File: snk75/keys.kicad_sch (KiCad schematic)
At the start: 255 parts

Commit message: Began routing
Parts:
- renumbered R12 to R10, R13 to R11, R14 to R12, R15 to R13, R16 to R14, R17 to R15, R18 to R16, R19 to R17, R20 to R18, R21 to R19, R22 to R20, R23 to R21, R24 to R22, R25 to R23, R26 to R24, R27 to R25, R28 to R26, R29 to R27, R30 to R28, R31 to R29, R32 to R30, R33 to R31, R34 to R32, R35 to R33, R36 to R34, R37 to R35, R38 to R36, R39 to R37, R40 to R38, R41 to R39, R42 to R40, R43 to R41, R44 to R42, R45 to R43, R46 to R44, R47 to R45, R48 to R46, R49 to R47, R50 to R48, R51 to R49, R52 to R50, R53 to R51, R54 to R52, R55 to R53, R56 to R54, R57 to R55, R58 to R56, R59 to R57, R60 to R58, R61 to R59, R62 to R60, R63 to R61, R64 to R62, R65 to R63, R66 to R64, R67 to R65, R68 to R66, R69 to R67, R70 to R68, R71 to R69, R72 to R70, R73 to R71, R74 to R72, R75 to R73, R76 to R74, R77 to R75, R78 to R76, R79 to R77, R80 to R78, R81 to R79, R10 to R8, R82 to R80, R83 to R81, R84 to R82, R85 to R83, R86 to R84, R87 to R85, R88 to R86, R89 to R87, R90 to R88, R91 to R89, R11 to R9, R92 to R90, R93 to R91, R94 to R92
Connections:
- net row1: no longer D7.1 (K)
- net at D7.2 (A): no longer MX7.2 (ROW)
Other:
- moved on the sheet: D7

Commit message: Changed MCU for STM32F072C8Tx and wired cols and rows
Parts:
- D1, D10, D11, D12, D13, D14, D15, D16, D17, D18, D19, D2, D20, D21, D22, D23, D24, D25, D26, D27, D28, D29, D3, D30, D31, D32, D33, D34, D35, D36, D37, D38, D39, D4, D40, D41, D42, D43, D44, D45, D46, D47, D48, D49, D5, D50, D51, D52, D53, D54, D55, D56, D57, D58, D59, D6, D60, D61, D62, D63, D64, D65, D66, D67, D68, D69, D7, D70, D71, D72, D73, D74, D75, D76, D77, D78, D79, D8, D80, D81, D82, D83, D84, D85, D9: footprint Diode_SMD:D_SOD-123 -> acheron_Components:D_SOD-123
- R10: renamed from R14; footprint Resistor_SMD:R_1206_3216Metric_Pad1.30x1.75mm_HandSolder -> Resistor_SMD:R_0402_1005Metric
- R11: renamed from R15; footprint Resistor_SMD:R_1206_3216Metric_Pad1.30x1.75mm_HandSolder -> Resistor_SMD:R_0402_1005Metric
- R12: renamed from R16; footprint Resistor_SMD:R_1206_3216Metric_Pad1.30x1.75mm_HandSolder -> Resistor_SMD:R_0402_1005Metric
- R13: renamed from R17; footprint Resistor_SMD:R_1206_3216Metric_Pad1.30x1.75mm_HandSolder -> Resistor_SMD:R_0402_1005Metric
- R14: renamed from R18; footprint Resistor_SMD:R_1206_3216Metric_Pad1.30x1.75mm_HandSolder -> Resistor_SMD:R_0402_1005Metric
- R15: renamed from R19; footprint Resistor_SMD:R_1206_3216Metric_Pad1.30x1.75mm_HandSolder -> Resistor_SMD:R_0402_1005Metric
- R16: renamed from R20; footprint Resistor_SMD:R_1206_3216Metric_Pad1.30x1.75mm_HandSolder -> Resistor_SMD:R_0402_1005Metric
- R17: renamed from R21; footprint Resistor_SMD:R_1206_3216Metric_Pad1.30x1.75mm_HandSolder -> Resistor_SMD:R_0402_1005Metric
- R18: renamed from R22; footprint Resistor_SMD:R_1206_3216Metric_Pad1.30x1.75mm_HandSolder -> Resistor_SMD:R_0402_1005Metric
- R19: renamed from R23; footprint Resistor_SMD:R_1206_3216Metric_Pad1.30x1.75mm_HandSolder -> Resistor_SMD:R_0402_1005Metric
- R20: renamed from R24; footprint Resistor_SMD:R_1206_3216Metric_Pad1.30x1.75mm_HandSolder -> Resistor_SMD:R_0402_1005Metric
- R21: renamed from R25; footprint Resistor_SMD:R_1206_3216Metric_Pad1.30x1.75mm_HandSolder -> Resistor_SMD:R_0402_1005Metric
- R22: renamed from R26; footprint Resistor_SMD:R_1206_3216Metric_Pad1.30x1.75mm_HandSolder -> Resistor_SMD:R_0402_1005Metric
- R23: renamed from R27; footprint Resistor_SMD:R_1206_3216Metric_Pad1.30x1.75mm_HandSolder -> Resistor_SMD:R_0402_1005Metric
- R24: renamed from R28; footprint Resistor_SMD:R_1206_3216Metric_Pad1.30x1.75mm_HandSolder -> Resistor_SMD:R_0402_1005Metric
- R25: renamed from R29; footprint Resistor_SMD:R_1206_3216Metric_Pad1.30x1.75mm_HandSolder -> Resistor_SMD:R_0402_1005Metric
- R26: renamed from R30; footprint Resistor_SMD:R_1206_3216Metric_Pad1.30x1.75mm_HandSolder -> Resistor_SMD:R_0402_1005Metric
- R27: renamed from R31; footprint Resistor_SMD:R_1206_3216Metric_Pad1.30x1.75mm_HandSolder -> Resistor_SMD:R_0402_1005Metric
- R28: renamed from R32; footprint Resistor_SMD:R_1206_3216Metric_Pad1.30x1.75mm_HandSolder -> Resistor_SMD:R_0402_1005Metric
- R29: renamed from R33; footprint Resistor_SMD:R_1206_3216Metric_Pad1.30x1.75mm_HandSolder -> Resistor_SMD:R_0402_1005Metric
- R30: renamed from R34; footprint Resistor_SMD:R_1206_3216Metric_Pad1.30x1.75mm_HandSolder -> Resistor_SMD:R_0402_1005Metric
- R31: renamed from R35; footprint Resistor_SMD:R_1206_3216Metric_Pad1.30x1.75mm_HandSolder -> Resistor_SMD:R_0402_1005Metric
- R32: renamed from R36; footprint Resistor_SMD:R_1206_3216Metric_Pad1.30x1.75mm_HandSolder -> Resistor_SMD:R_0402_1005Metric
- R33: renamed from R37; footprint Resistor_SMD:R_1206_3216Metric_Pad1.30x1.75mm_HandSolder -> Resistor_SMD:R_0402_1005Metric
- R34: renamed from R38; footprint Resistor_SMD:R_1206_3216Metric_Pad1.30x1.75mm_HandSolder -> Resistor_SMD:R_0402_1005Metric
- R35: renamed from R39; footprint Resistor_SMD:R_1206_3216Metric_Pad1.30x1.75mm_HandSolder -> Resistor_SMD:R_0402_1005Metric
- R36: renamed from R40; footprint Resistor_SMD:R_1206_3216Metric_Pad1.30x1.75mm_HandSolder -> Resistor_SMD:R_0402_1005Metric
- R37: renamed from R41; footprint Resistor_SMD:R_1206_3216Metric_Pad1.30x1.75mm_HandSolder -> Resistor_SMD:R_0402_1005Metric
- R38: renamed from R42; footprint Resistor_SMD:R_1206_3216Metric_Pad1.30x1.75mm_HandSolder -> Resistor_SMD:R_0402_1005Metric
- R39: renamed from R43; footprint Resistor_SMD:R_1206_3216Metric_Pad1.30x1.75mm_HandSolder -> Resistor_SMD:R_0402_1005Metric
- R4: renamed from R8; footprint Resistor_SMD:R_1206_3216Metric_Pad1.30x1.75mm_HandSolder -> Resistor_SMD:R_0402_1005Metric
- R40: renamed from R44; footprint Resistor_SMD:R_1206_3216Metric_Pad1.30x1.75mm_HandSolder -> Resistor_SMD:R_0402_1005Metric
- R41: renamed from R45; footprint Resistor_SMD:R_1206_3216Metric_Pad1.30x1.75mm_HandSolder -> Resistor_SMD:R_0402_1005Metric
- R42: renamed from R46; footprint Resistor_SMD:R_1206_3216Metric_Pad1.30x1.75mm_HandSolder -> Resistor_SMD:R_0402_1005Metric
- R43: renamed from R47; footprint Resistor_SMD:R_1206_3216Metric_Pad1.30x1.75mm_HandSolder -> Resistor_SMD:R_0402_1005Metric
- R44: renamed from R48; footprint Resistor_SMD:R_1206_3216Metric_Pad1.30x1.75mm_HandSolder -> Resistor_SMD:R_0402_1005Metric
- R45: renamed from R49; footprint Resistor_SMD:R_1206_3216Metric_Pad1.30x1.75mm_HandSolder -> Resistor_SMD:R_0402_1005Metric
- R46: renamed from R50; footprint Resistor_SMD:R_1206_3216Metric_Pad1.30x1.75mm_HandSolder -> Resistor_SMD:R_0402_1005Metric
- R47: renamed from R51; footprint Resistor_SMD:R_1206_3216Metric_Pad1.30x1.75mm_HandSolder -> Resistor_SMD:R_0402_1005Metric
- R48: renamed from R52; footprint Resistor_SMD:R_1206_3216Metric_Pad1.30x1.75mm_HandSolder -> Resistor_SMD:R_0402_1005Metric
- R49: renamed from R53; footprint Resistor_SMD:R_1206_3216Metric_Pad1.30x1.75mm_HandSolder -> Resistor_SMD:R_0402_1005Metric
- R5: renamed from R9; footprint Resistor_SMD:R_1206_3216Metric_Pad1.30x1.75mm_HandSolder -> Resistor_SMD:R_0402_1005Metric
- R50: renamed from R54; footprint Resistor_SMD:R_1206_3216Metric_Pad1.30x1.75mm_HandSolder -> Resistor_SMD:R_0402_1005Metric
- R51: renamed from R55; footprint Resistor_SMD:R_1206_3216Metric_Pad1.30x1.75mm_HandSolder -> Resistor_SMD:R_0402_1005Metric
- R52: renamed from R56; footprint Resistor_SMD:R_1206_3216Metric_Pad1.30x1.75mm_HandSolder -> Resistor_SMD:R_0402_1005Metric
- R53: renamed from R57; footprint Resistor_SMD:R_1206_3216Metric_Pad1.30x1.75mm_HandSolder -> Resistor_SMD:R_0402_1005Metric
- R54: renamed from R58; footprint Resistor_SMD:R_1206_3216Metric_Pad1.30x1.75mm_HandSolder -> Resistor_SMD:R_0402_1005Metric
- R55: renamed from R59; footprint Resistor_SMD:R_1206_3216Metric_Pad1.30x1.75mm_HandSolder -> Resistor_SMD:R_0402_1005Metric
- R56: renamed from R60; footprint Resistor_SMD:R_1206_3216Metric_Pad1.30x1.75mm_HandSolder -> Resistor_SMD:R_0402_1005Metric
- R57: renamed from R61; footprint Resistor_SMD:R_1206_3216Metric_Pad1.30x1.75mm_HandSolder -> Resistor_SMD:R_0402_1005Metric
- R58: renamed from R62; footprint Resistor_SMD:R_1206_3216Metric_Pad1.30x1.75mm_HandSolder -> Resistor_SMD:R_0402_1005Metric
- R59: renamed from R63; footprint Resistor_SMD:R_1206_3216Metric_Pad1.30x1.75mm_HandSolder -> Resistor_SMD:R_0402_1005Metric
- R6: renamed from R10; footprint Resistor_SMD:R_1206_3216Metric_Pad1.30x1.75mm_HandSolder -> Resistor_SMD:R_0402_1005Metric
- R60: renamed from R64; footprint Resistor_SMD:R_1206_3216Metric_Pad1.30x1.75mm_HandSolder -> Resistor_SMD:R_0402_1005Metric
- R61: renamed from R65; footprint Resistor_SMD:R_1206_3216Metric_Pad1.30x1.75mm_HandSolder -> Resistor_SMD:R_0402_1005Metric
- R62: renamed from R66; footprint Resistor_SMD:R_1206_3216Metric_Pad1.30x1.75mm_HandSolder -> Resistor_SMD:R_0402_1005Metric
- R63: renamed from R67; footprint Resistor_SMD:R_1206_3216Metric_Pad1.30x1.75mm_HandSolder -> Resistor_SMD:R_0402_1005Metric
- R64: renamed from R68; footprint Resistor_SMD:R_1206_3216Metric_Pad1.30x1.75mm_HandSolder -> Resistor_SMD:R_0402_1005Metric
- R65: renamed from R69; footprint Resistor_SMD:R_1206_3216Metric_Pad1.30x1.75mm_HandSolder -> Resistor_SMD:R_0402_1005Metric
- R66: renamed from R70; footprint Resistor_SMD:R_1206_3216Metric_Pad1.30x1.75mm_HandSolder -> Resistor_SMD:R_0402_1005Metric
- R67: renamed from R71; footprint Resistor_SMD:R_1206_3216Metric_Pad1.30x1.75mm_HandSolder -> Resistor_SMD:R_0402_1005Metric
- R68: renamed from R72; footprint Resistor_SMD:R_1206_3216Metric_Pad1.30x1.75mm_HandSolder -> Resistor_SMD:R_0402_1005Metric
- R69: renamed from R73; footprint Resistor_SMD:R_1206_3216Metric_Pad1.30x1.75mm_HandSolder -> Resistor_SMD:R_0402_1005Metric
- R7: renamed from R11; footprint Resistor_SMD:R_1206_3216Metric_Pad1.30x1.75mm_HandSolder -> Resistor_SMD:R_0402_1005Metric
- R70: renamed from R74; footprint Resistor_SMD:R_1206_3216Metric_Pad1.30x1.75mm_HandSolder -> Resistor_SMD:R_0402_1005Metric
- R71: renamed from R75; footprint Resistor_SMD:R_1206_3216Metric_Pad1.30x1.75mm_HandSolder -> Resistor_SMD:R_0402_1005Metric
- R72: renamed from R76; footprint Resistor_SMD:R_1206_3216Metric_Pad1.30x1.75mm_HandSolder -> Resistor_SMD:R_0402_1005Metric
- R73: renamed from R77; footprint Resistor_SMD:R_1206_3216Metric_Pad1.30x1.75mm_HandSolder -> Resistor_SMD:R_0402_1005Metric
- R74: renamed from R78; footprint Resistor_SMD:R_1206_3216Metric_Pad1.30x1.75mm_HandSolder -> Resistor_SMD:R_0402_1005Metric
- R75: renamed from R79; footprint Resistor_SMD:R_1206_3216Metric_Pad1.30x1.75mm_HandSolder -> Resistor_SMD:R_0402_1005Metric
- R76: renamed from R80; footprint Resistor_SMD:R_1206_3216Metric_Pad1.30x1.75mm_HandSolder -> Resistor_SMD:R_0402_1005Metric
- R77: renamed from R81; footprint Resistor_SMD:R_1206_3216Metric_Pad1.30x1.75mm_HandSolder -> Resistor_SMD:R_0402_1005Metric
- R78: renamed from R82; footprint Resistor_SMD:R_1206_3216Metric_Pad1.30x1.75mm_HandSolder -> Resistor_SMD:R_0402_1005Metric
- R79: renamed from R83; footprint Resistor_SMD:R_1206_3216Metric_Pad1.30x1.75mm_HandSolder -> Resistor_SMD:R_0402_1005Metric
- R8: renamed from R12; footprint Resistor_SMD:R_1206_3216Metric_Pad1.30x1.75mm_HandSolder -> Resistor_SMD:R_0402_1005Metric
- R80: renamed from R84; footprint Resistor_SMD:R_1206_3216Metric_Pad1.30x1.75mm_HandSolder -> Resistor_SMD:R_0402_1005Metric
- R81: renamed from R85; footprint Resistor_SMD:R_1206_3216Metric_Pad1.30x1.75mm_HandSolder -> Resistor_SMD:R_0402_1005Metric
- R82: renamed from R86; footprint Resistor_SMD:R_1206_3216Metric_Pad1.30x1.75mm_HandSolder -> Resistor_SMD:R_0402_1005Metric
- R83: renamed from R87; footprint Resistor_SMD:R_1206_3216Metric_Pad1.30x1.75mm_HandSolder -> Resistor_SMD:R_0402_1005Metric
- R84: renamed from R88; footprint Resistor_SMD:R_1206_3216Metric_Pad1.30x1.75mm_HandSolder -> Resistor_SMD:R_0402_1005Metric
- R85: renamed from R89; footprint Resistor_SMD:R_1206_3216Metric_Pad1.30x1.75mm_HandSolder -> Resistor_SMD:R_0402_1005Metric
- R86: renamed from R90; footprint Resistor_SMD:R_1206_3216Metric_Pad1.30x1.75mm_HandSolder -> Resistor_SMD:R_0402_1005Metric
- R87: renamed from R91; footprint Resistor_SMD:R_1206_3216Metric_Pad1.30x1.75mm_HandSolder -> Resistor_SMD:R_0402_1005Metric
- R88: renamed from R92; footprint Resistor_SMD:R_1206_3216Metric_Pad1.30x1.75mm_HandSolder -> Resistor_SMD:R_0402_1005Metric
- R9: renamed from R13; footprint Resistor_SMD:R_1206_3216Metric_Pad1.30x1.75mm_HandSolder -> Resistor_SMD:R_0402_1005Metric
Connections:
- net col15: now also MX82.1 (COL)
- net row1: now also D7.1 (K)
- net at D7.2 (A): now also MX7.2 (ROW)
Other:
- moved on the sheet: D7

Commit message: added new row layout and connected row1 to MCU
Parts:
- renumbered R12 to R10, R13 to R11, R14 to R12, R15 to R13, R16 to R14, R17 to R15, R18 to R16, R19 to R17, R20 to R18, R21 to R19, R4 to R2, R22 to R20, R23 to R21, R24 to R22, R25 to R23, R26 to R24, R27 to R25, R28 to R26, R29 to R27, R30 to R28, R31 to R29, R5 to R3, R32 to R30, R33 to R31, R34 to R32, R35 to R33, R36 to R34, R37 to R35, R38 to R36, R39 to R37, R40 to R38, R41 to R39, R6 to R4, R42 to R40, R43 to R41, R44 to R42, R45 to R43, R46 to R44, R47 to R45, R48 to R46, R49 to R47, R50 to R48, R51 to R49, R7 to R5, R52 to R50, R53 to R51, R54 to R52, R55 to R53, R56 to R54, R57 to R55, R58 to R56, R59 to R57, R60 to R58, R61 to R59, R8 to R6, R62 to R60, R63 to R61, R64 to R62, R65 to R63, R66 to R64, R67 to R65, R68 to R66, R69 to R67, R70 to R68, R71 to R69, R9 to R7, R72 to R70, R73 to R71, R74 to R72, R75 to R73, R76 to R74, R77 to R75, R78 to R76, R79 to R77, R80 to R78, R81 to R79, R10 to R8, R82 to R80, R83 to R81, R84 to R82, R85 to R83, R86 to R84, R87 to R85, R88 to R86, R11 to R9

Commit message: added components on board and began routing
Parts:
- renumbered R2 to R1, R11 to R10, R12 to R11, R13 to R12, R14 to R13, R15 to R14, R16 to R15, R17 to R16, R18 to R17, R19 to R18, R20 to R19, R3 to R2, R21 to R20, R22 to R21, R23 to R22, R24 to R23, R25 to R24, R26 to R25, R27 to R26, R28 to R27, R29 to R28, R30 to R29, R4 to R3, R31 to R30, R32 to R31, R33 to R32, R34 to R33, R35 to R34, R36 to R35, R37 to R36, R38 to R37, R39 to R38, R40 to R39, R5 to R4, R41 to R40, R42 to R41, R43 to R42, R44 to R43, R45 to R44, R46 to R45, R47 to R46, R48 to R47, R49 to R48, R50 to R49, R6 to R5, R51 to R50, R52 to R51, R53 to R52, R54 to R53, R55 to R54, R56 to R55, R57 to R56, R58 to R57, R59 to R58, R60 to R59, R7 to R6, R61 to R60, R62 to R61, R63 to R62, R64 to R63, R65 to R64, R66 to R65, R67 to R66, R68 to R67, R69 to R68, R70 to R69, R8 to R7, R71 to R70, R72 to R71, R73 to R72, R74 to R73, R75 to R74, R76 to R75, R77 to R76, R78 to R77, R79 to R78, R80 to R79, R9 to R8, R81 to R80, R82 to R81, R83 to R82, R84 to R83, R85 to R84, R86 to R85, R10 to R9

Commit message: Nearly make all paths
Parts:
- D1, D10, D11, D12, D13, D14, D15, D16, D17, D18, D19, D2, D20, D21, D22, D23, D24, D25, D26, D27, D28, D29, D3, D30, D31, D32, D33, D34, D35, D36, D37, D38, D39, D4, D40, D41, D42, D43, D44, D45, D46, D47, D48, D49, D5, D50, D51, D52, D53, D54, D55, D56, D57, D58, D59, D6, D60, D61, D62, D63, D64, D65, D66, D67, D68, D69, D7, D70, D71, D72, D73, D74, D75, D76, D77, D78, D79, D8, D80, D81, D82, D83, D84, D85, D9: value 1N14148W -> 1N4148W; JLCPCB BOM (none) -> 1; LCSC (none) -> C81598; LCSC Part (none) -> C81598; LCSC Part Number (none) -> C81598
- MX1, MX10, MX11, MX12, MX13, MX14, MX15, MX16, MX17, MX18, MX19, MX2, MX20, MX21, MX22, MX23, MX24, MX25, MX26, MX27, MX28, MX29, MX3, MX30, MX31, MX32, MX33, MX34, MX35, MX36, MX37, MX38, MX39, MX4, MX40, MX41, MX42, MX43, MX44, MX45, MX46, MX47, MX48, MX49, MX5, MX50, MX51, MX52, MX53, MX54, MX55, MX56, MX57, MX58, MX59, MX6, MX60, MX61, MX62, MX63, MX64, MX65, MX66, MX67, MX68, MX69, MX7, MX70, MX71, MX72, MX73, MX74, MX75, MX76, MX77, MX78, MX79, MX8, MX80, MX81, MX82, MX83, MX84, MX85, MX9: JLCPCB BOM (none) -> 0
- R1, R10, R11, R12, R13, R14, R15, R16, R17, R18, R19, R2, R20, R21, R22, R23, R24, R25, R26, R27, R28, R29, R3, R30, R31, R32, R33, R34, R35, R36, R37, R38, R39, R4, R40, R41, R42, R43, R44, R45, R46, R47, R48, R49, R5, R50, R51, R52, R53, R54, R55, R56, R57, R58, R59, R6, R60, R61, R62, R63, R64, R65, R66, R67, R68, R69, R7, R70, R71, R72, R73, R74, R75, R76, R77, R78, R79, R8, R80, R81, R82, R83, R84, R85, R9: JLCPCB BOM (none) -> 1; LCSC C23228 -> C433827; LCSC Part (none) -> C433827; LCSC Part Number (none) -> C433827

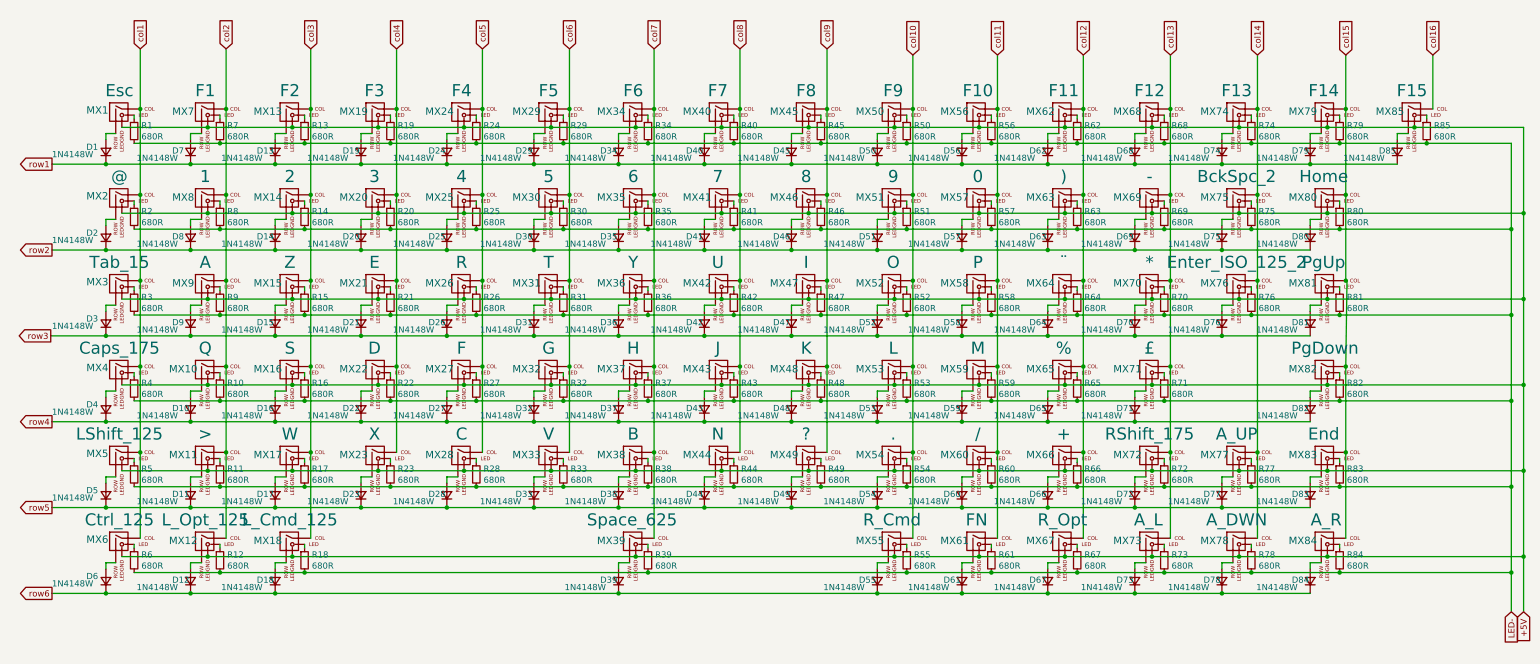
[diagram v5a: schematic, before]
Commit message: WIP: replacing backlight LEDs with RGB LEDs
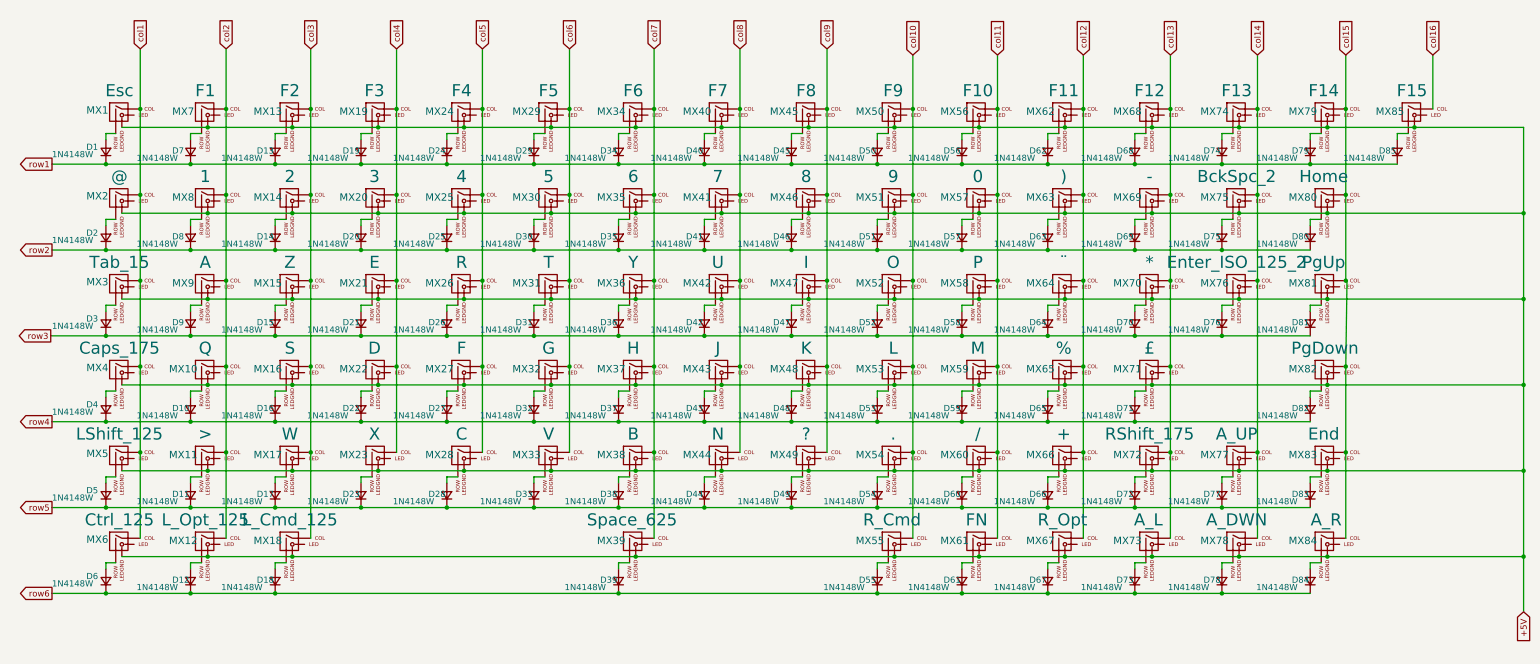
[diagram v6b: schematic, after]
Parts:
- removed R1, R10, R11, R12, R13, R14, R15, R16, R17, R18, R19, R2, R20, R21, R22, R23, R24, R25, R26, R27, R28, R29, R3, R30, R31, R32, R33, R34, R35, R36, R37, R38, R39, R4, R40, R41, R42, R43, R44, R45, R46, R47, R48, R49, R5, R50, R51, R52, R53, R54, R55, R56, R57, R58, R59, R6, R60, R61, R62, R63, R64, R65, R66, R67, R68, R69, R7, R70, R71, R72, R73, R74, R75, R76, R77, R78, R79, R8, R80, R81, R82, R83, R84, R85, R9: 680R, Resistor_SMD:R_0402_1005Metric, symbol Device:R_Small
- MX1, MX10, MX11, MX13, MX14, MX15, MX16, MX17, MX19, MX2, MX20, MX21, MX22, MX23, MX24, MX25, MX26, MX27, MX28, MX29, MX30, MX31, MX32, MX33, MX34, MX35, MX36, MX37, MX38, MX40, MX41, MX42, MX43, MX44, MX45, MX46, MX47, MX48, MX49, MX50, MX51, MX52, MX53, MX54, MX55, MX56, MX57, MX58, MX59, MX60, MX61, MX62, MX63, MX64, MX65, MX66, MX67, MX68, MX69, MX7, MX70, MX71, MX73, MX74, MX77, MX78, MX79, MX8, MX80, MX81, MX82, MX83, MX84, MX85, MX9: footprint MX_Only:MXOnly-1U -> MX_Only:MXOnly-1U-NoLED
- MX12, MX18, MX5, MX6: footprint MX_Only:MXOnly-1.25U -> MX_Only:MXOnly-1.25U-NoLED
- MX3: footprint MX_Only:MXOnly-1.5U -> MX_Only:MXOnly-1.5U-NoLED
- MX39: footprint MX_Only:MXOnly-6.25U -> MX_Only:MXOnly-6.25U-NoLED
- MX4, MX72: footprint MX_Only:MXOnly-1.75U -> MX_Only:MXOnly-1.75U-NoLED
- MX75: footprint MX_Only:MXOnly-2U -> MX_Only:MXOnly-2U-NoLED
- MX76: footprint MX_Only:MXOnly-ISO -> MX_Only:MXOnly-ISO-NoLED
